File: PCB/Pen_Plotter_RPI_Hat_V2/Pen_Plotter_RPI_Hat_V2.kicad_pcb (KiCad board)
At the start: 2 copper layers, 85 x 56 mm, 43 parts, among them U1 ATmega328P-P, U2 BIDIRECTIONAL_LEVEL_SHIFTER_7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, U3 MINI560_5V, U4 X-AXIS_DRV8825_STEPPER_MOTOR_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, U5 Y-AXIS_DRV8825_STEPPER_MOTOR_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, U6 RPI3-MODBP-BULK, U7 LM393AN, Y1 X322516MLB4SI

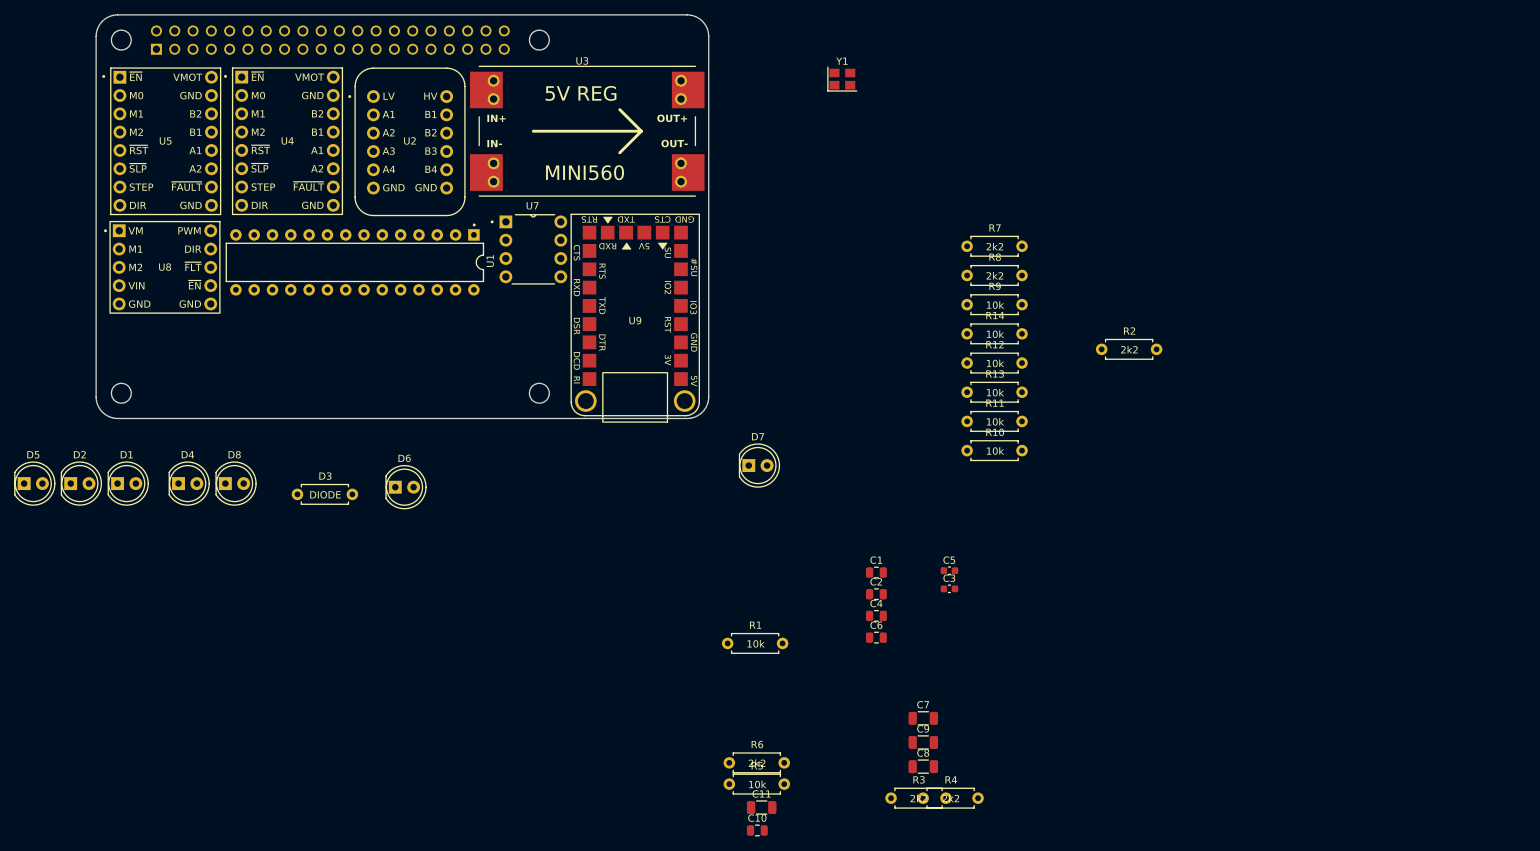
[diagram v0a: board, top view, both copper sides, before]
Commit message: Simplified design, began layout process
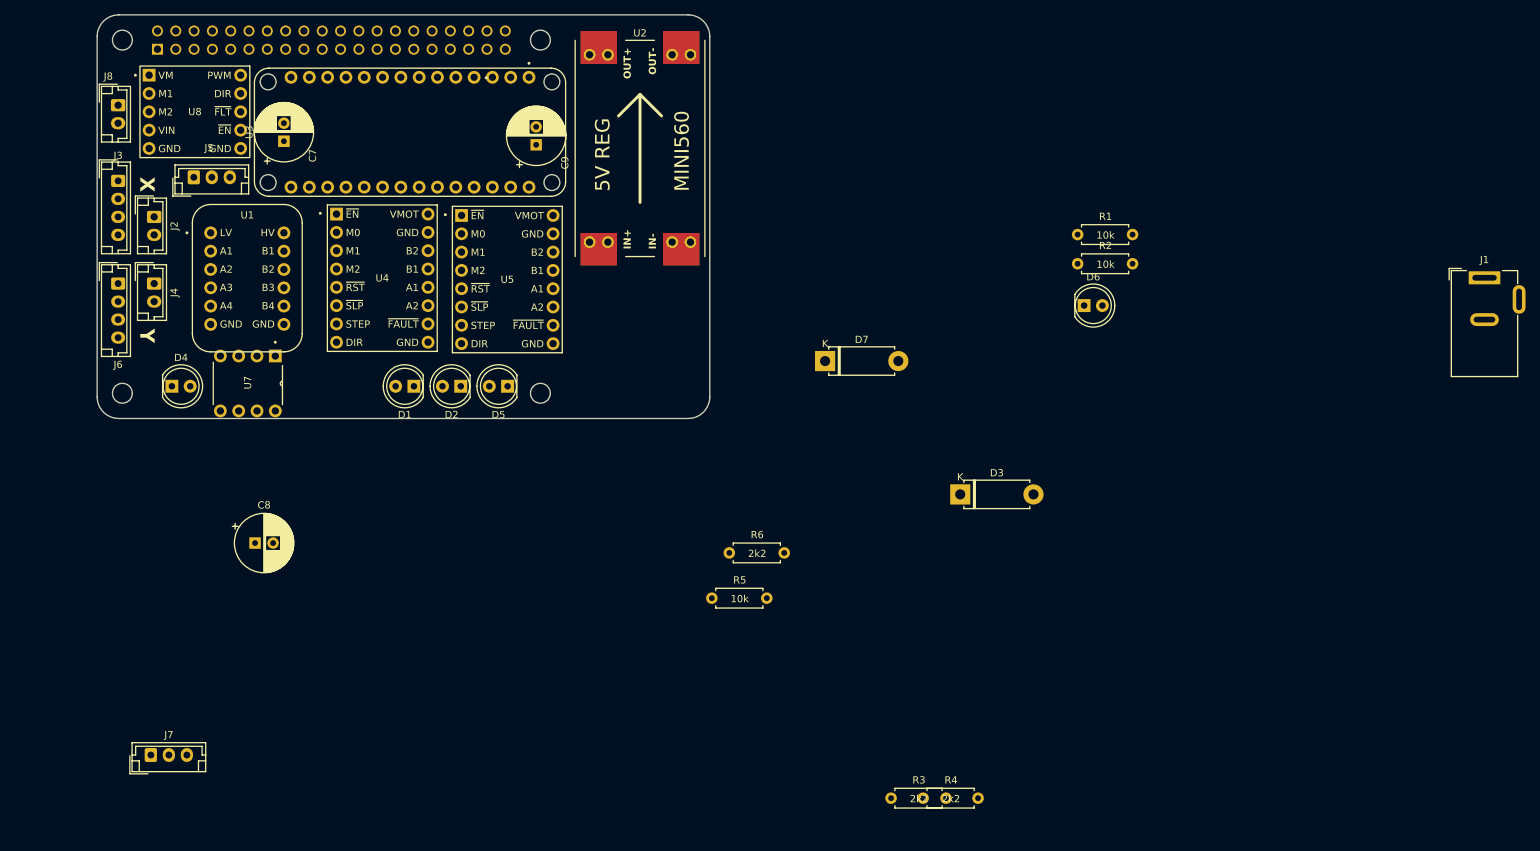
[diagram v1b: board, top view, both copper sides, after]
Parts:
- removed C1, C2, C4, C6: 100n, Capacitor_SMD:C_0805_2012Metric
- removed C10: 1u, Capacitor_SMD:C_0805_2012Metric
- removed C11: 100u, Capacitor_SMD:C_1206_3216Metric
- removed C3, C5: 10p, Capacitor_SMD:C_0603_1608Metric
- removed D8: GREEN, LED_THT:LED_D5.0mm
- removed R10, R11, R12, R13, R14, R9: 10k, Pen_Plotter_Lib:THT_RESISTOR_WITH_VALUE
- removed R7, R8: 2k2, Pen_Plotter_Lib:THT_RESISTOR_WITH_VALUE
- removed U9: ~, Pen_Plotter_Lib:CP2102N_FRIEND_CARRIER_BOARD_SMD
- removed Y1: X322516MLB4SI, Crystal:Crystal_SMD_3225-4Pin_3.2x2.5mm
- added J1: BARREL_JACK_12V, Connector_BarrelJack:BarrelJack_Wuerth_6941xx301002, F.Cu at (248.6, 71.0)
- added J2: X_LIMIT_SWITCH, Connector_JST:JST_EH_B2B-EH-A_1x02_P2.50mm_Vertical, F.Cu at (64.0, 62.5)
- added J3: X-AXIS_STEPPER, Connector_JST:JST_EH_B4B-EH-A_1x04_P2.50mm_Vertical, F.Cu at (59.0, 57.5)
- added J4: Y_LIMIT_SWITCH, Connector_JST:JST_EH_B2B-EH-A_1x02_P2.50mm_Vertical, F.Cu at (64.0, 71.8)
- added J5: SERVO, Connector_JST:JST_EH_B3B-EH-A_1x03_P2.50mm_Vertical, F.Cu at (69.5, 57.0)
- added J6: Y-AXIS_STEPPER, Connector_JST:JST_EH_B4B-EH-A_1x04_P2.50mm_Vertical, F.Cu at (59.0, 71.8)
- added J7: PAPER_SENSOR, Connector_JST:JST_EH_B3B-EH-A_1x03_P2.50mm_Vertical, F.Cu at (63.5, 137.2)
- added J8: DC_MOTOR, Connector_JST:JST_EH_B2B-EH-A_1x02_P2.50mm_Vertical, F.Cu at (59.0, 47.0)
- C7, C8, C9: footprint Capacitor_SMD:C_1206_3216Metric -> Capacitor_THT:CP_Radial_D8.0mm_P2.50mm
- D3: footprint Pen_Plotter_Lib:THT_RESISTOR_WITH_VALUE -> Diode_THT:D_5W_P10.16mm_Horizontal
- D6: value YELLOW -> GREEN
- D7: value YELLOW -> DIODE; footprint LED_THT:LED_D5.0mm -> Diode_THT:D_5W_P10.16mm_Horizontal
- R2: value 2k2 -> 10k
- U1: value ATmega328P-P -> BIDIRECTIONAL_LEVEL_SHIFTER_757; footprint Package_DIP:DIP-28_W7.62mm -> Pen_Plotter_Lib:BIDIRECTIONAL_LEVEL_SHIFTER_575
- U2: value BIDIRECTIONAL_LEVEL_SHIFTER_757 -> MINI560; footprint Pen_Plotter_Lib:BIDIRECTIONAL_LEVEL_SHIFTER_575 -> Pen_Plotter_Lib:MINI560_5V
- U3: value MINI560_5V -> METRO_MINI_2590; footprint Pen_Plotter_Lib:MINI560_5V -> Pen_Plotter_Lib:METRO_MINI_MODULE_2590
- moved C7 119.5 mm to (82.0, 52.0), turned to 90 degrees
- moved D6 98.8 mm to (193.0, 74.8)
- moved C9 98.8 mm to (117.0, 52.5), turned to 90 degrees
- moved C8 97.8 mm to (78.0, 107.8)
- moved D3 88.1 mm to (175.8, 101.0)
- moved R1 74.7 mm to (196.0, 65.0)
- moved D5 68.4 mm to (113.0, 86.0), turned to 180 degrees
- moved D2 55.8 mm to (106.5, 86.0), turned to 180 degrees
- moved U5 51.1 mm to (113.0, 71.2)
- moved U7 50.8 mm to (73.2, 89.4), turned to -90 degrees
- moved U2 43.9 mm to (140.4, 68.0), turned to 90 degrees
- moved D1 43.3 mm to (100.0, 86.0), turned to 180 degrees
- moved U1 32.0 mm to (76.9, 71.0), turned to 0 degrees
- moved R6 29.1 mm to (147.7, 109.2)
- moved R5 25.9 mm to (145.2, 115.5)
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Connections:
- D4 pad 1: /Raspberry Pi/PAPER_SENSOR_OUT_LED_NEG -> PAPER_SENSOR_OUT_5V
- D4 pad 2: PAPER_SENSOR_OUT_5V -> /Raspberry Pi/PAPER_SENSOR_OUT_LED_POS
- D6 pad 2: +5V -> Net-(D6-A)
- R1 pad 1: MCU_RESET -> MCU_RX
- R2 pad 1: +12V -> GND
- R2 pad 2: Net-(U3-EN) -> Net-(D6-K)
- R5 pad 1: GND -> +5V
- R5 pad 2: /Raspberry Pi/PAPER_SENSOR_OUT_LED_NEG -> /Raspberry Pi/PAPER_SENSOR_OUT_LED_POS
- U3 pad 1: Net-(U3-EN) -> Net-(D6-A)
- U3 pad 2: +12V -> MCU_RESET
- U3 pad 3: GND -> unconnected-(U3-3.3V-Pad3)
- U3 pad 4: +5V -> Net-(D7-K)
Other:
- board text added: "X"
- board text added: "Y"

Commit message: Completed PCB component layout, routing and silkscreen work is still needed
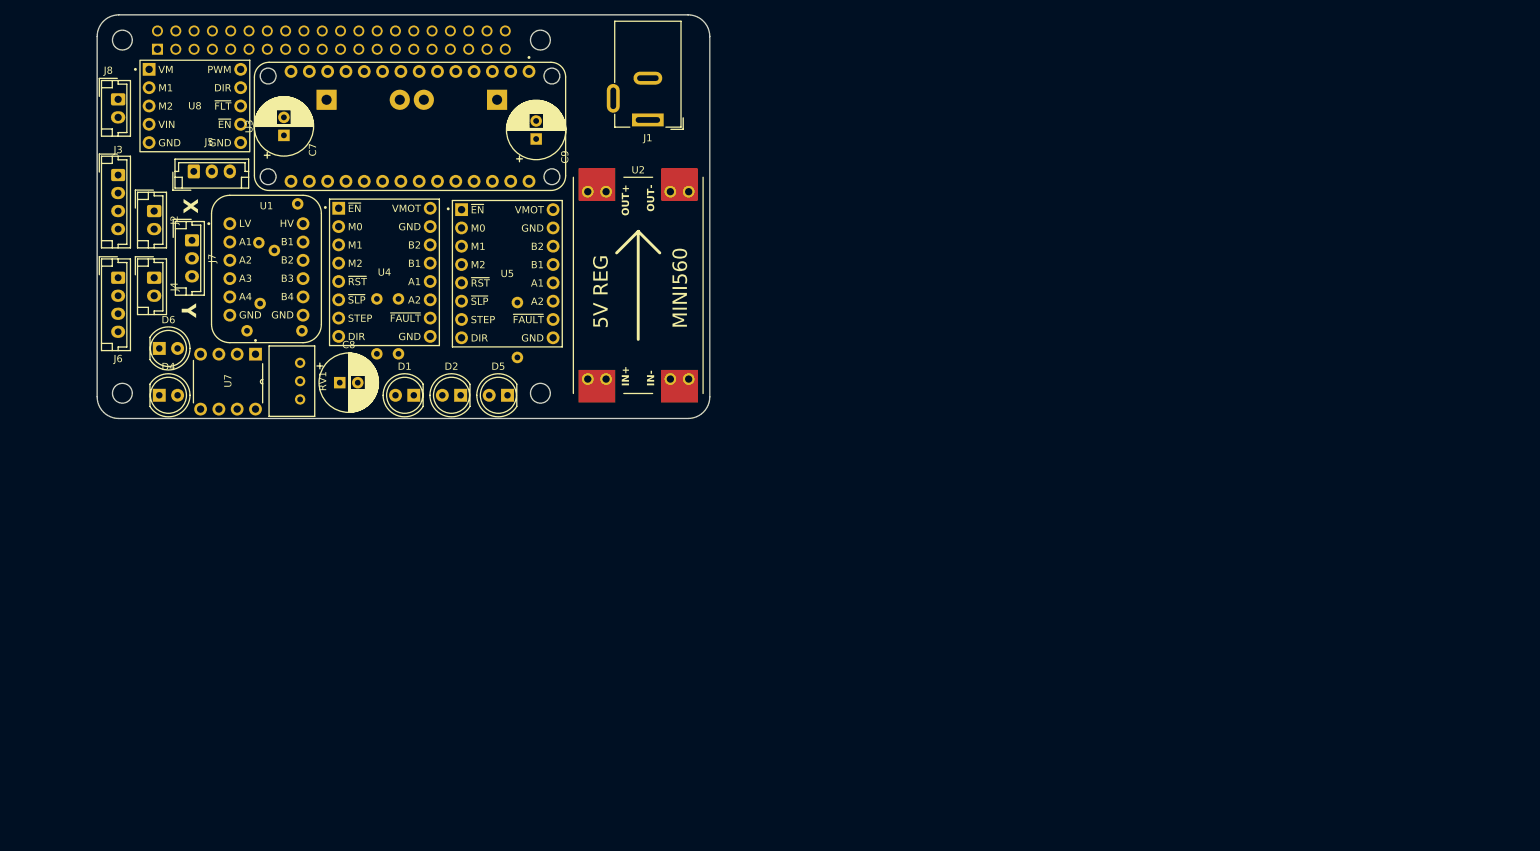
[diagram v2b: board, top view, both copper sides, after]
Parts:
- added RV1: PAPER_SENSOR_POT, Potentiometer_THT:Potentiometer_Bourns_3299W_Vertical, F.Cu at (84.2, 87.8)
- D3, D7, R1, R2, R3, R4, R5, R6: moved to B.Cu
- moved D6 128.5 mm to (64.7, 80.8)
- moved J1 118.1 mm to (132.5, 49.0), turned to 180 degrees
- moved R2 115.7 mm to (80.6, 78.4), turned to 180 degrees
- moved R1 114.8 mm to (81.2, 63.5), turned to -135 degrees
- moved D3 103.6 mm to (87.9, 46.2)
- moved R4 100.8 mm to (98.0, 77.8), turned to -90 degrees
- moved R3 99.7 mm to (95.0, 77.8), turned to -90 degrees
- moved R5 79.2 mm to (79.8, 70.9), turned to -105 degrees
- moved J7 71.6 mm to (69.2, 65.8), turned to -90 degrees
- moved D7 58.2 mm to (111.6, 46.2), turned to 180 degrees
- moved R6 45.4 mm to (114.5, 78.2), turned to -90 degrees
- moved C8 25.2 mm to (89.8, 85.5)
- moved U2 19.0 mm to (140.2, 87.0)
- moved U1 2.95 mm to (79.6, 69.7)
- moved U7 2.76 mm to (70.4, 89.2)
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
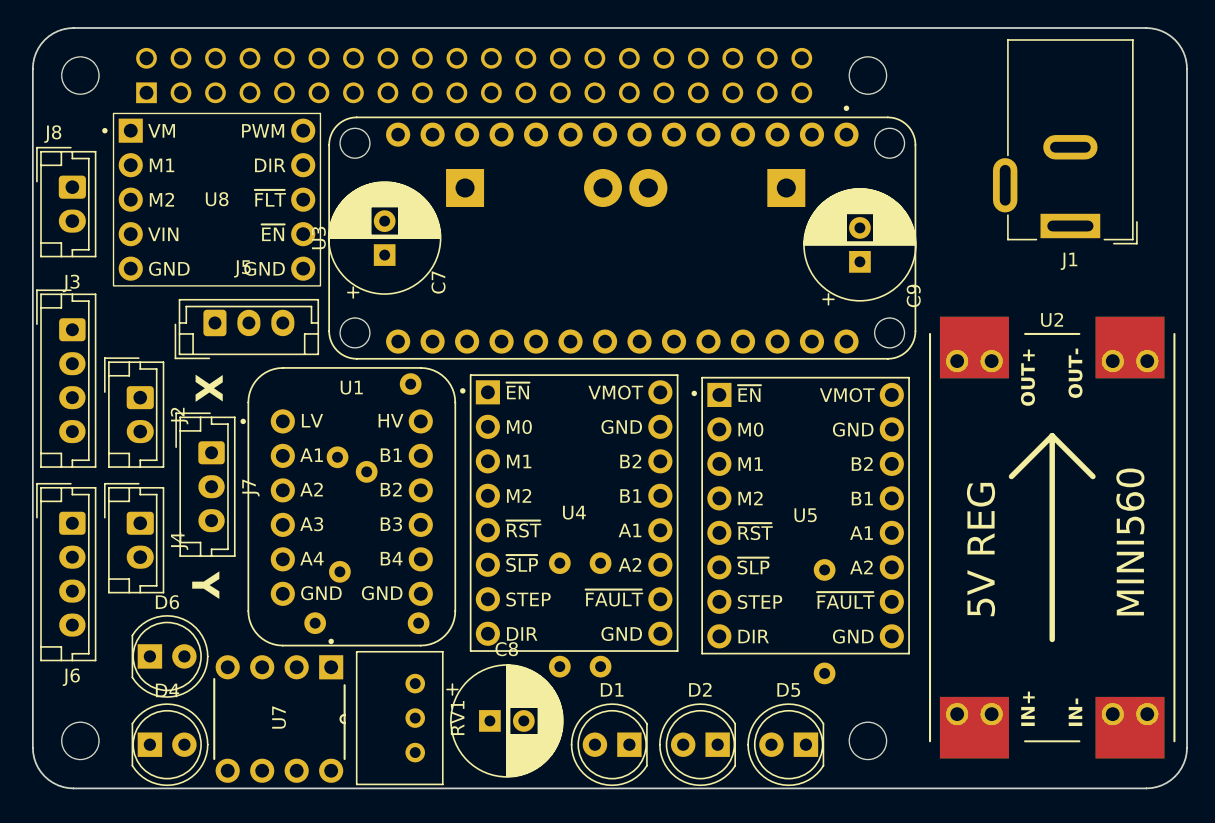
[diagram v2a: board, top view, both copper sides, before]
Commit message: Completed PCB layout, started routing
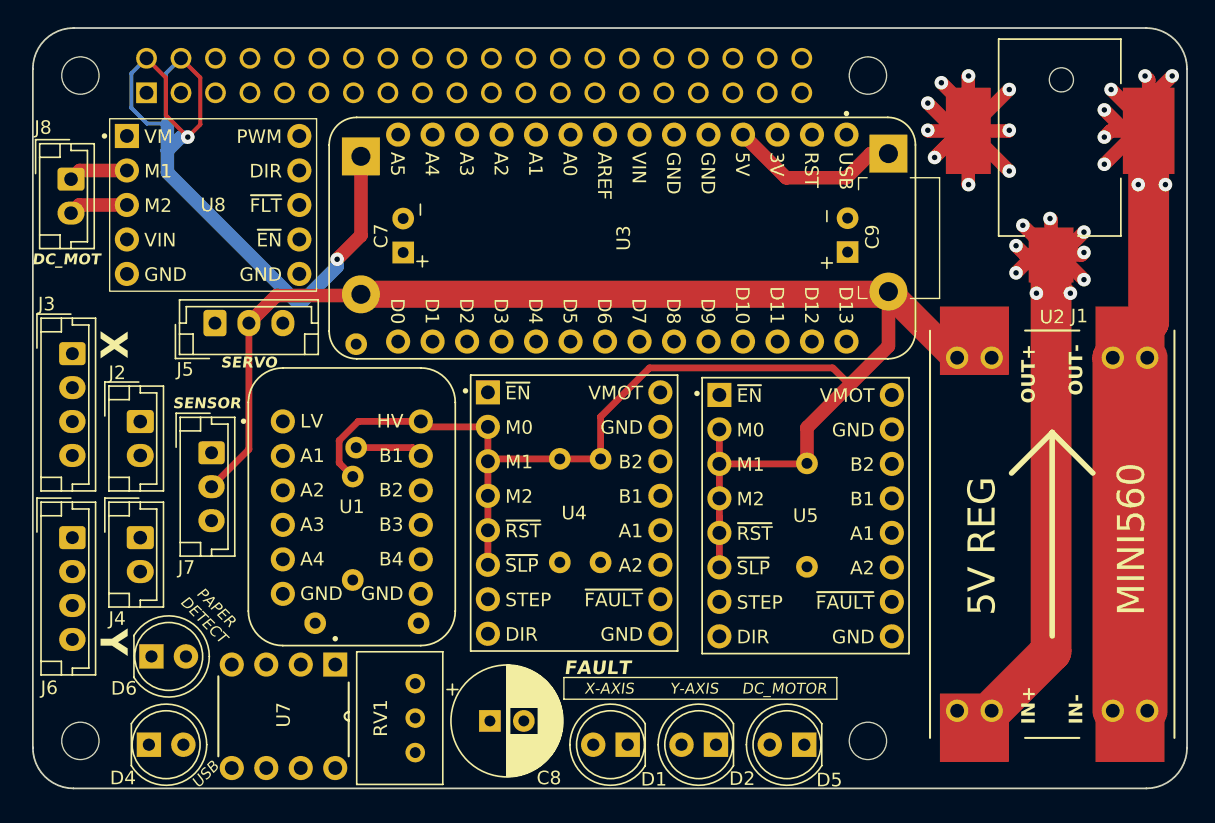
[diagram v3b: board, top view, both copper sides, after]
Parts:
- J1: value BARREL_JACK_12V -> RASM712PX; footprint Connector_BarrelJack:BarrelJack_Wuerth_6941xx301002 -> Pen_Plotter_Lib:SWITCHCRAFT_RASM712PX
- moved D3 8.02 mm to (80.2, 43.9), turned to -90 degrees
- moved R6 7.96 mm to (113.2, 70.4)
- moved D7 7.93 mm to (119.1, 43.7), turned to -90 degrees
- moved R3 7.68 mm to (95.0, 70.1)
- moved R4 7.68 mm to (98.0, 70.1)
- moved J1 7.04 mm to (131.8, 42.0)
- moved R1 2.26 mm to (80.0, 61.6), turned to -90 degrees
- moved J2 1.76 mm to (64.0, 63.5)
- moved J3 1.76 mm to (59.0, 58.5)
- moved C7 1.38 mm to (83.4, 51.0)
- moved C9 1.16 mm to (116.1, 51.0)
- moved J4 1.06 mm to (64.0, 72.0)
- moved J6 1.06 mm to (59.0, 72.0)
- moved J8 0.60 mm to (58.9, 45.6)
- moved U8 0.48 mm to (69.4, 47.5)
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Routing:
- net +5V: track 0.00 -> 158.0 mm
- net GND: track 0.00 -> 137.5 mm, vias 0 -> 17
- net +12V: track 0.00 -> 60.8 mm, vias 0 -> 9
- net Net-(D3-K): track 0.00 -> 58.2 mm, vias 0 -> 2
- net Net-(D7-K): track 0.00 -> 12.8 mm
- net Net-(R1-Pad2): track 0.00 -> 5.01 mm
- net Net-(J8-Pin_1): track 0.00 -> 4.38 mm
- net Net-(J8-Pin_2): track 0.00 -> 4.36 mm
- added copper zone on In2.Cu, net +12V
- added copper zone on In1.Cu, net GND
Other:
- copper layers 2 -> 4
- board text added: "DC_MOT"
- board text added: "DC_MOTOR"
- board text added: "FAULT"
- board text added: "PAPER DETECT"
- board text added: "SENSOR"
- board text added: "SERVO"
- board text added: "USB"
- board text added: "X-AXIS"
- board text added: "Y-AXIS"
